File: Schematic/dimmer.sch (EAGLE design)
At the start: 19 parts, among them T1 SPP20N6055-N, T3 BC547, X1 W237-102°45_00

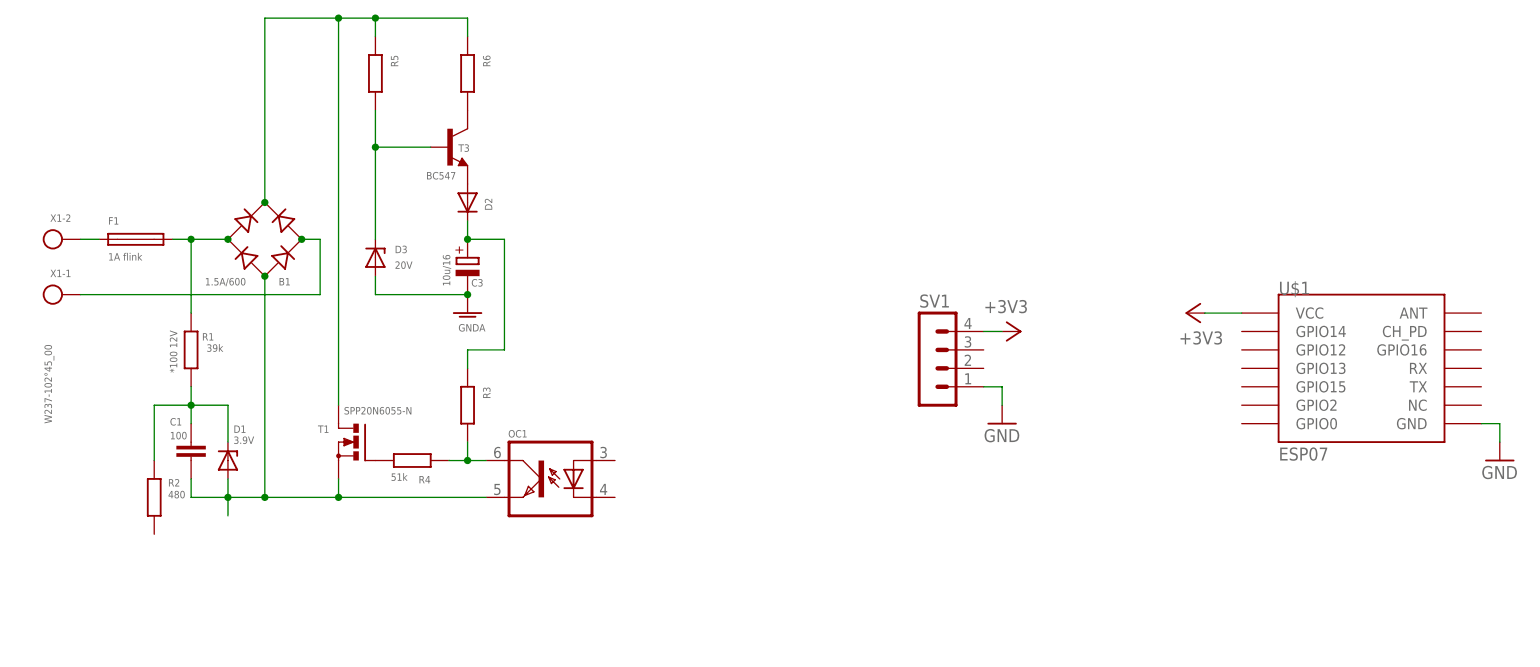
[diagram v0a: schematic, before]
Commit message: Add board size
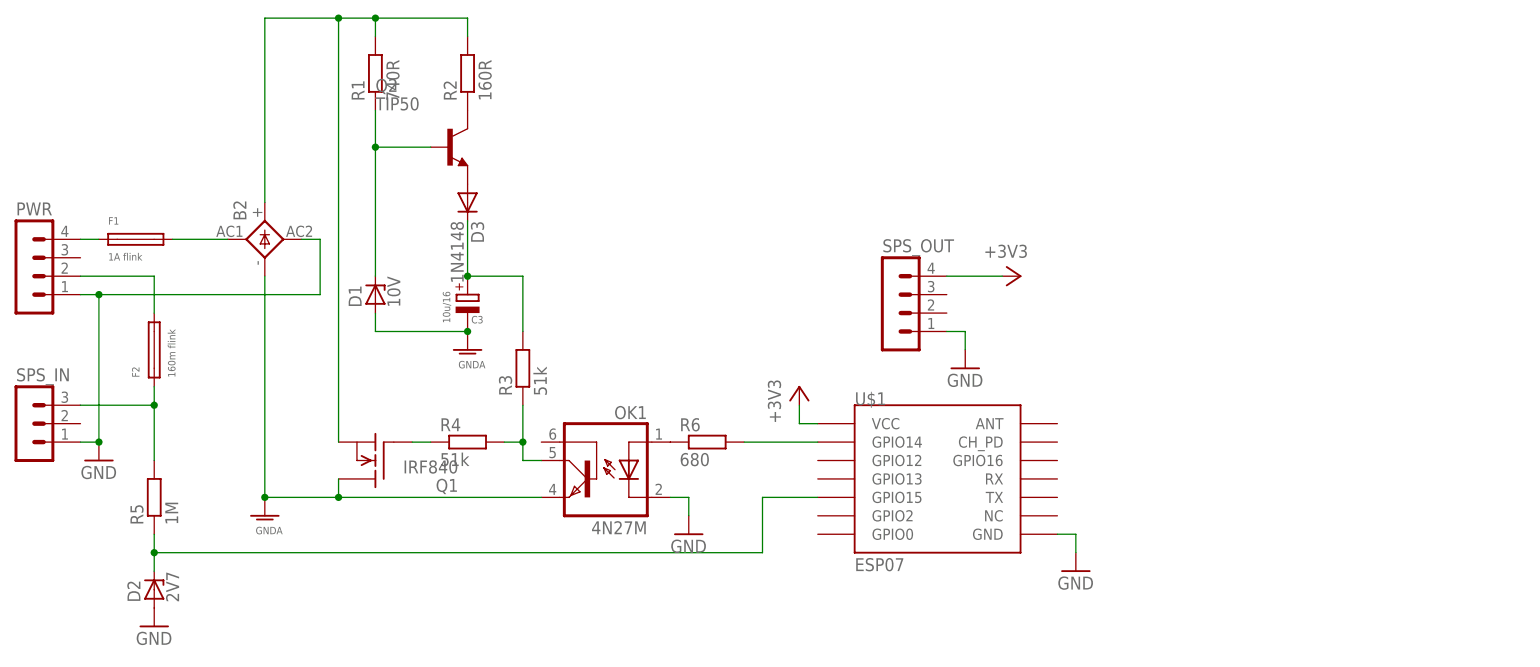
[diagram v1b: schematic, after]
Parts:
- removed B1: 1.5A/600, rectifier:RB1A
- removed C1: 100, rcl:C-EU050-025X075
- removed SV1: (no value), con-lstb:MA04-1
- removed T1: SPP20N6055-N, transistor-power:SPP20N6055-N
- removed T3: BC547, transistor-npn:BC547
- removed U$3: OC1, optocoupler:ILD205SOCI08-N
- removed X1: W237-102°45_00, con-wago-500:W237-102°45_00
- added B2: (no value), rectifier:2KBP
- added F2: 160m flink, fuse:19560
- added OK1: 4N27M, optocoupler:4N27M
- added PWR, SPS_OUT: (no value), con-lstb:MA04-1
- added Q1: IRF840, transistor-fet:IRF840
- added Q2: TIP50, transistor-npn:BD705
- added SPS_IN: (no value), con-lstb:MA03-1
- D1: value 3.9V -> 10V; device diode:BZX90SMD -> diode:ZENER-DIODEF126-12
- D2: value (none) -> 2V7; device diode:DIODE-D-7.5 -> diode:ZENER-DIODEF126-12
- D3: value 20V -> 1N4148; device diode:BZX90N -> diode:1N4148DO35-7
- R1: value 39k -> 740R; device rcl:R-EU_0204/12 -> rcl:R-EU_0207/12
- R2: value 480 -> 160R; device rcl:R-EU_M1206 -> rcl:R-EU_0207/12
- R3: value (none) -> 51k; device rcl:R-EU_M1206 -> rcl:R-EU_0207/12
- R4: device rcl:R-EU_M1206 -> rcl:R-EU_0207/12
- R5: value (none) -> 1M; device rcl:R-EU_M1206 -> rcl:R-EU_0207/12
- R6: value (none) -> 680; device rcl:R-EU_M1206 -> rcl:R-EU_0207/12
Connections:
- removed net N$30: C1.1, D1.C, R1.2, R2.2
- new net N$10: D2.C, R5.1, U$1.GPIO15
- new net N$12: R6.2, U$1.GPIO14
- new net N$8: F2.2, PWR.2
- new net N$9: F2.1, R5.2, SPS_IN.3
- net +3V3: now also SPS_OUT.4; no longer SV1.4
- net GND: now also B2.AC2, D2.A, OK1.C, PWR.1, SPS_IN.1, SPS_OUT.1; no longer SV1.1
- net GNDA: now also B2.-, OK1.EMI, Q1.D; no longer B1.-, C1.2, D3.A, T1.S, U$3G$2.EMIT
- net N$1: now also Q1.G, R4.1; no longer R4.2, T1.G
- net N$17: now also B2.AC1; no longer B1.AC1, R1.1
- net N$2: now also OK1.COL, R3.1, R4.2; no longer R3.2, R4.1, U$3G$2.COL
- net N$21: now also B2.+, Q1.S, R1.2, R2.2; no longer B1.+, R5.1, R6.1, T1.D
- net N$3: now also Q2.C, R2.1; no longer B1.AC2, X1-1.KL
- net N$31: now also PWR.4; no longer X1-2.KL
- net N$4: now also D3.A, Q2.E; no longer R6.2, T3.C
- net N$5: now also D1.C, Q2.B, R1.1; no longer D3.C, R5.2, T3.B
- net N$6: now also OK1.A, R6.1; no longer D2.A, T3.E
- net N$7: now also D3.C, R3.2; no longer D2.C, R3.1
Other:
- note removed: "*100 12V"
- moved on the sheet: C3, R1, R2, R3, R4, R5, R6, U$1
